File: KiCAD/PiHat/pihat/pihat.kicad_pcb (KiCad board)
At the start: 2 copper layers, 64.8 x 55.9 mm, 39 parts, among them J1 Pan Servo Connector, J2 Tilt Servo Connector, J3 Fan, J4 Power Connector, P1 Conn_02x20_Odd_Even, P4 Pad, Q1 BSS138, Q2 BSS138, U1 TPS5430-Q1, U2 TMP36xS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

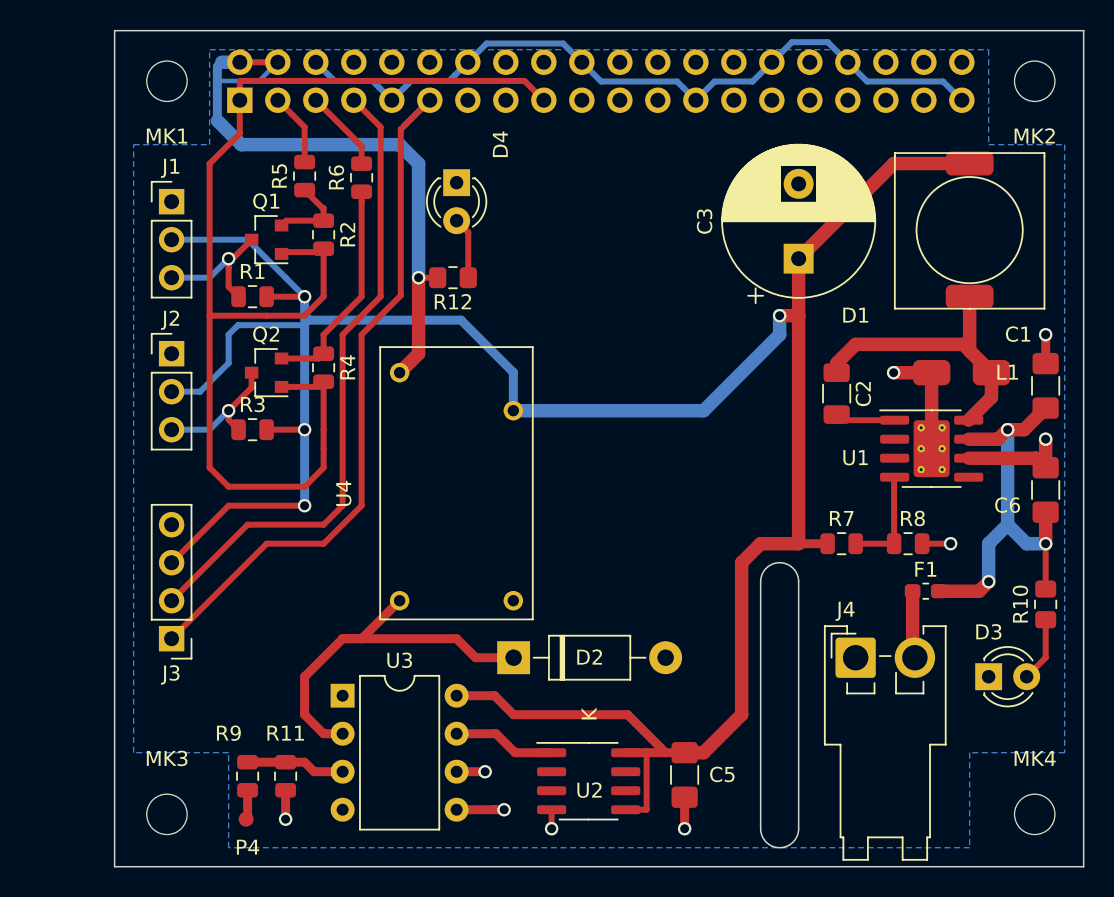
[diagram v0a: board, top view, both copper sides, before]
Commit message: Added MOSFET switch, Logo, Prototype area
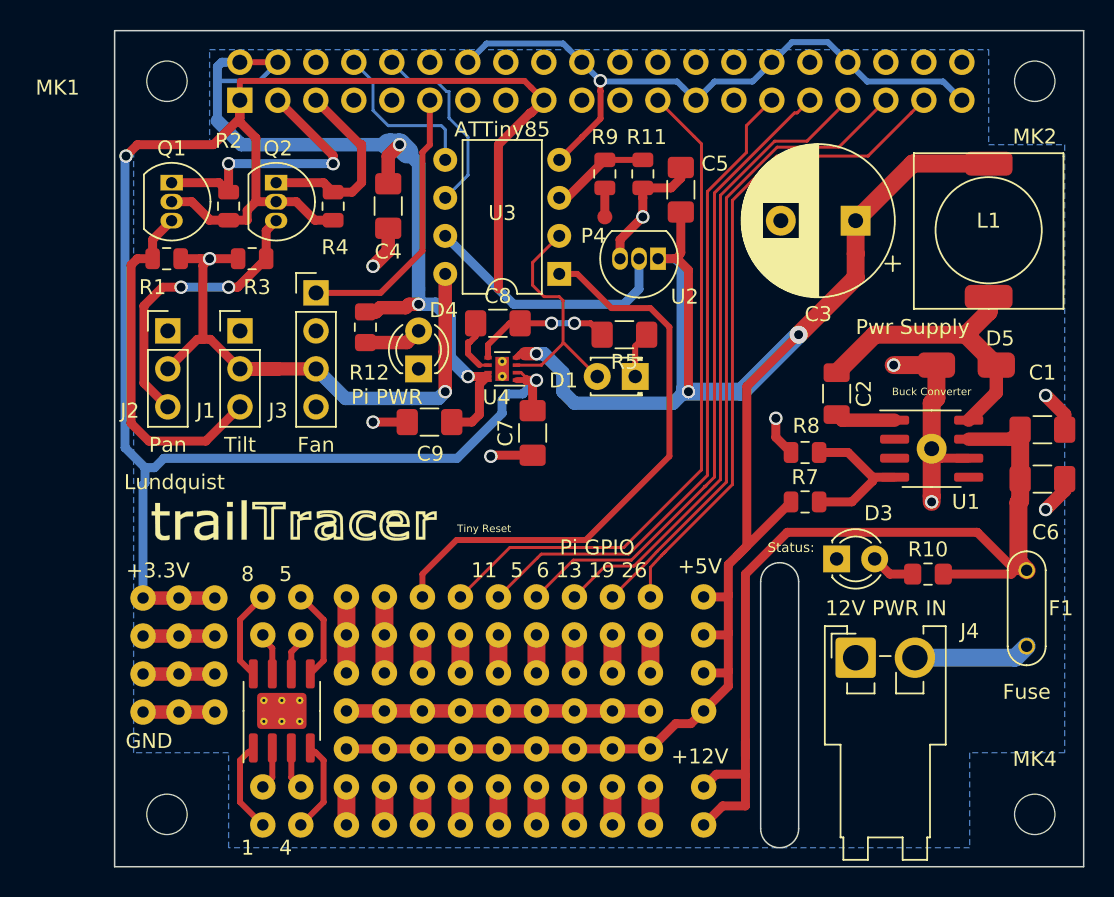
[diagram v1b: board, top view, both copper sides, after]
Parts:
- removed D2: 1N4001, Diode_THT:D_DO-41_SOD81_P10.16mm_Horizontal
- removed R6: 220R, Resistor_SMD:R_0805_2012Metric
- added  : Hole, trailTracer:Hole, F.Cu at (201.9, 129.5)
- added  : Hole, trailTracer:Hole, F.Cu at (204.3, 129.5)
- added  : SOIC_IO, trailTracer:SOIC_IO, F.Cu at (212.4, 149.7)
- added  : SOIC_IO, trailTracer:SOIC_IO, F.Cu at (209.9, 129.4)
- added  : SOIC-8-1EP_3.9x4.9mm_P1.27mm_EP2.41x3.3mm_ThermalVias, Package_SO:SOIC-8-1EP_3.9x4.9mm_P1.27mm_EP2.41x3.3mm_ThermalVias, F.Cu at (211.2, 139.6)
- added  : Breadbord layout, trailTracer:Breadbord layout, F.Cu at (215.5, 126.9)
- added +12V: Holes_2, trailTracer:Holes_2, F.Cu at (239.4, 142.1)
- added +3.3V: Hole, trailTracer:Hole, F.Cu at (206.7, 129.5)
- added +5V: Hole, trailTracer:Hole, F.Cu at (239.4, 129.4)
- added C4: 220 uF, Capacitor_SMD:C_1206_3216Metric_Pad1.42x1.75mm_HandSolder, F.Cu at (218.3, 105.8)
- added C7: 100uF, Resistor_SMD:R_1206_3216Metric_Pad1.42x1.75mm_HandSolder, F.Cu at (227.9, 121.0)
- added C8: 220pF, Resistor_SMD:R_1206_3216Metric_Pad1.42x1.75mm_HandSolder, F.Cu at (225.6, 113.7)
- added C9: 10uF, Resistor_SMD:R_1206_3216Metric_Pad1.42x1.75mm_HandSolder, F.Cu at (221.0, 120.3)
- added D5: B340, trailTracer:B340, F.Cu at (258.9, 116.5)
- added G***: LOGO, trailTracer:Logo, F.Cu at (211.6, 128.9)
-  : renamed from MK3
- D1: value B340 -> LED; footprint trailTracer:DO-214 -> LED_THT:LED_D1.8mm_W3.3mm_H2.4mm
- F1: value 5A Medium Blow -> Fuse; footprint Resistor_SMD:R_0603_1608Metric_Pad1.05x0.95mm_HandSolder -> trailTracer:Fuse_Holder_TR5
- Q1, Q2: value BSS138 -> 2N7000; footprint Package_TO_SOT_SMD:SOT-23 -> Package_TO_SOT_THT:TO-92_Inline
- R5: footprint Resistor_SMD:R_0805_2012Metric -> Resistor_SMD:R_1206_3216Metric_Pad1.42x1.75mm_HandSolder
- U1: footprint Package_SO:SOIC-8-1EP_3.9x4.9mm_P1.27mm_EP2.41x3.81mm_ThermalVias -> trailTracer:SOIC-8-1EP_3.9x4.9mm_P1.27mm_EP2.29x3mm_ThermalVias
- U2: value TMP36xS -> LMT87; footprint Package_SO:SOIC-8_3.9x4.9mm_P1.27mm -> Package_TO_SOT_THT:TO-92_Inline
- U4: value TE_OJ-SH-105LM -> TPS22965; footprint trailTracer:TE_OJ-SH-105LM -> Package_SON:WSON-8-1EP_2x2mm_P0.5mm_EP0.9x1.6mm_ThermalVias
- moved R11 46.8 mm to (235.3, 103.7)
- moved R9 46.8 mm to (232.8, 103.7)
- moved P4 46.7 mm to (232.8, 106.7), turned to 0 degrees
- moved C5 39.1 mm to (237.8, 104.8), turned to 90 degrees
- moved U2 35.2 mm to (236.3, 109.4), turned to 180 degrees
- moved U3 31.7 mm to (229.7, 110.4), turned to 180 degrees
- moved J3 25.0 mm to (213.5, 111.6), turned to 0 degrees
- moved R5 23.9 mm to (234.1, 114.4), turned to 180 degrees
- moved D1 23.8 mm to (234.8, 117.2)
- moved D3 12.9 mm to (248.3, 129.4)
- moved Q2 12.7 mm to (210.8, 104.3), turned to 270 degrees
- moved D4 12.7 mm to (220.3, 116.7), turned to 90 degrees
- moved U4 11.7 mm to (225.9, 116.7), turned to 180 degrees
- moved R3 11.4 mm to (209.2, 109.4), turned to 180 degrees
- moved R4 10.8 mm to (214.6, 105.9)
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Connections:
- D1 pad 1: Net-(C2-Pad1) -> Net-(D1-Pad1)
- D1 pad 2: GND -> TINY_B4
- J3 pad 2: GPIO_4 -> Net-(J3-Pad2)
- P1 pad 10: GPIO_15 -> TINY_B1
- P1 pad 8: GPIO_14 -> TINY_B0
- Q1 pad 1: +3V3 -> GPIO_2
- Q1 pad 2: Net-(Q1-Pad2) -> +3V3
- Q2 pad 1: +3V3 -> GPIO_3
- Q2 pad 2: Net-(Q2-Pad2) -> +3V3
- R2 pad 1: Net-(Q1-Pad2) -> GPIO_2
- R4 pad 1: Net-(Q2-Pad2) -> GPIO_3
- R5 pad 1: Net-(Q1-Pad2) -> Net-(D1-Pad1)
- R5 pad 2: GPIO_2 -> GND
- U2 pad 1: TINY_B2 -> +5V
- U2 pad 2: (no net) -> TINY_B2
- U2 pad 3: (no net) -> GND
- U3 pad 5: GPIO_15 -> TINY_B0
- U3 pad 6: GPIO_14 -> TINY_B1
- U4 pad 1: TINY_B4 -> +3V3
- U4 pad 2: GND -> +3V3
- U4 pad 3: +5V -> TINY_B4
- U4 pad 4: PI_5V -> +5V
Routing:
- net (no net): track 0.00 -> 87.2 mm
- net +3V3: track 78.6 -> 135.1 mm, vias 0 -> 2
- net GPIO_11: track 0.00 -> 45.5 mm
- net /GPIO26: track 0.00 -> 44.6 mm
- net /GPIO5: track 0.00 -> 44.2 mm
- net GND: track 74.8 -> 118.6 mm, vias 7 -> 12
- net /GPIO6: track 0.00 -> 43.3 mm
- net /GPIO19(SPI1_MISO): track 0.00 -> 43.2 mm
- net GPIO_13: track 0.00 -> 43.2 mm
- net GPIO_4: track 43.0 -> 0.00 mm
- net Net-(U3-Pad1): track 0.00 -> 38.8 mm
- net +12V: track 28.5 -> 62.6 mm, vias 3 -> 0
- net GPIO_17: track 47.8 -> 18.7 mm
- net Net-(Q2-Pad2): track 14.8 -> 0.00 mm
- net Net-(J1-Pad3): track 9.22 -> 24.0 mm, vias 1 -> 0
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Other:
- board text added: "1"
- board text added: "11 5 6 13 19 26"
- board text added: "12V PWR IN"
- board text added: "4"
- board text added: "5"
- board text added: "8"
- board text added: "ATTiny85"
- board text added: "Buck Converter"
- board text added: "Fan"
- board text added: "Fuse"
- board text added: "GND"
- board text added: "Lundquist"
- board text added: "Pan"
- board text added: "Pi GPIO"
- board text added: "Pi PWR"
- board text added: "Pwr Supply"
- board text added: "Status:"
- board text added: "Tilt"
- board text added: "Tiny Reset"
- board text removed: "RASPBERRY-PI 40-PIN ADDON BOARD VIEW FROM TOP NOTE: P1 SHOULD BE FITTED ON THE REVERSE OF THE BOARD ADD EDGE CUTS FROM CAMERA AND DISPLAY PORTS AS REQUIRED"
